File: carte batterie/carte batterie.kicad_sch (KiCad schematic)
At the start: 11 parts, among them IC1 TPS3711DDCT, J1 Conn_01x02_Pin, J2 Conn_01x02_Pin, J3 Conn_01x01_Pin, Q1 SI3127DV-T1-GE3, U1 ATtiny1616-S

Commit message: new compo
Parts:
- added IC2: TPS54531DDA, SOIC127P600X170-9N, symbol SamacSys_Parts:TPS54531DDA
- R4: value R -> 330
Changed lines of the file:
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@@
       (effects (font (size 1.27 1.27)) (justify left))
     )
-    (property "Value" "R" (at 54.61 104.775 0)
+    (property "Value" "330" (at 54.61 104.775 0)
       (effects (font (size 1.27 1.27)) (justify left))
     )
@@
         )
       )
+    )
+  )
+  (symbol (lib_id "SamacSys_Parts:TPS54531DDA") (at 103.505 129.54 0) (unit 1)
+    (in_bom yes) (on_board yes) (dnp no) (fields_autoplaced)
+    (property "Reference" "IC2" (at 118.745 121.92 0)
+      (effects (font (size 1.27 1.27)))
+    )
+    (property "Value" "TPS54531DDA" (at 118.745 124.46 0)
+      (effects (font (size 1.27 1.27)))
+    )
+    (property "Footprint" "SOIC127P600X170-9N" (at 130.175 224.46 0)
+      (effects (font (size 1.27 1.27)) (justify left top) hide)
+    )
+    (property "Datasheet" "http://www.ti.com/lit/gpn/tps54531" (at 130.175 324.46 0)
+      (effects (font (size 1.27 1.27)) (justify left top) hide)
+    )
+    (property "Height" "1.7" (at 130.175 524.46 0)
+      (effects (font (size 1.27 1.27)) (justify left top) hide)
+    )
+    (property "Manufacturer_Name" "Texas Instruments" (at 130.175 624.46 0)
+      (effects (font (size 1.27 1.27)) (justify left top) hide)
+    )
+    (property "Manufacturer_Part_Number" "TPS54531DDA" (at 130.175 724.46 0)
+      (effects (font (size 1.27 1.27)) (justify left top) hide)
+    )
+    (property "Mouser Part Number" "595-TPS54531DDA" (at 130.175 824.46 0)
+      (effects (font (size 1.27 1.27)) (justify left top) hide)
+    )
+    (property "Mouser Price/Stock" "https://www.mouser.co.uk/ProductDetail/Texas-Instruments/TPS54531DDA?qs=jA5Ki6243omoJVKISZs%2FBg%3D%3D" (at 130.175 924.46 0)
+      (effects (font (size 1.27 1.27)) (justify left top) hide)
+    )
+    (property "Arrow Part Number" "TPS54531DDA" (at 130.175 1024.46 0)
+      (effects (font (size 1.27 1.27)) (justify left top) hide)
+    )
+    (property "Arrow Price/Stock" "https://www.arrow.com/en/products/tps54531dda/texas-instruments?region=nac" (at 130.175 1124.46 0)
+      (effects (font (size 1.27 1.27)) (justify left top) hide)
+    )
+    (pin "1")
+    (pin "2")
+    (pin "3")
+    (pin "4")
+    (pin "5")
+    (pin "6")
+    (pin "7")
+    (pin "8")
+    (pin "9")
+    (instances
+      (project "carte batterie"
+        (path "/8afff8df-3578-4f51-814d-4ef430aba141"
+          (reference "IC2") (unit 1)
+        )
+      )

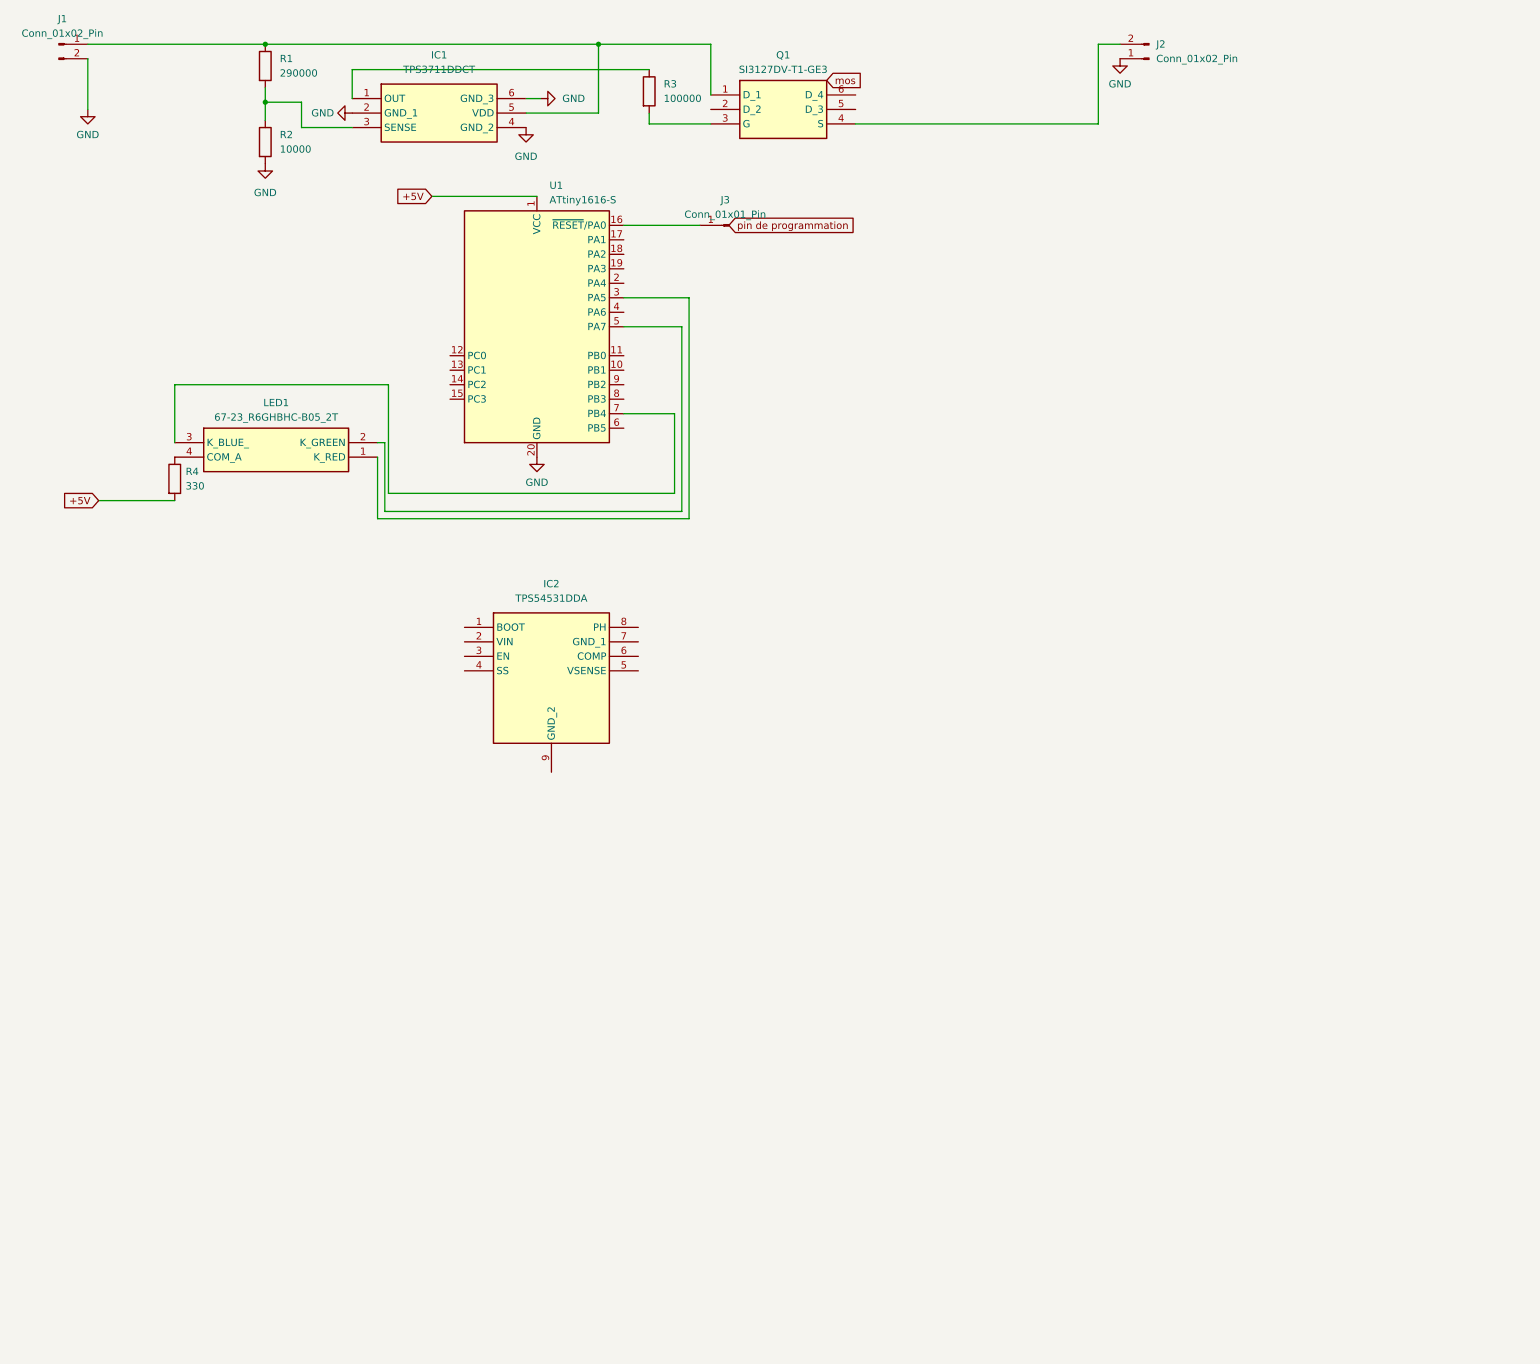
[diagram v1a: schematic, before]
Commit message: ajout ref carte batterie
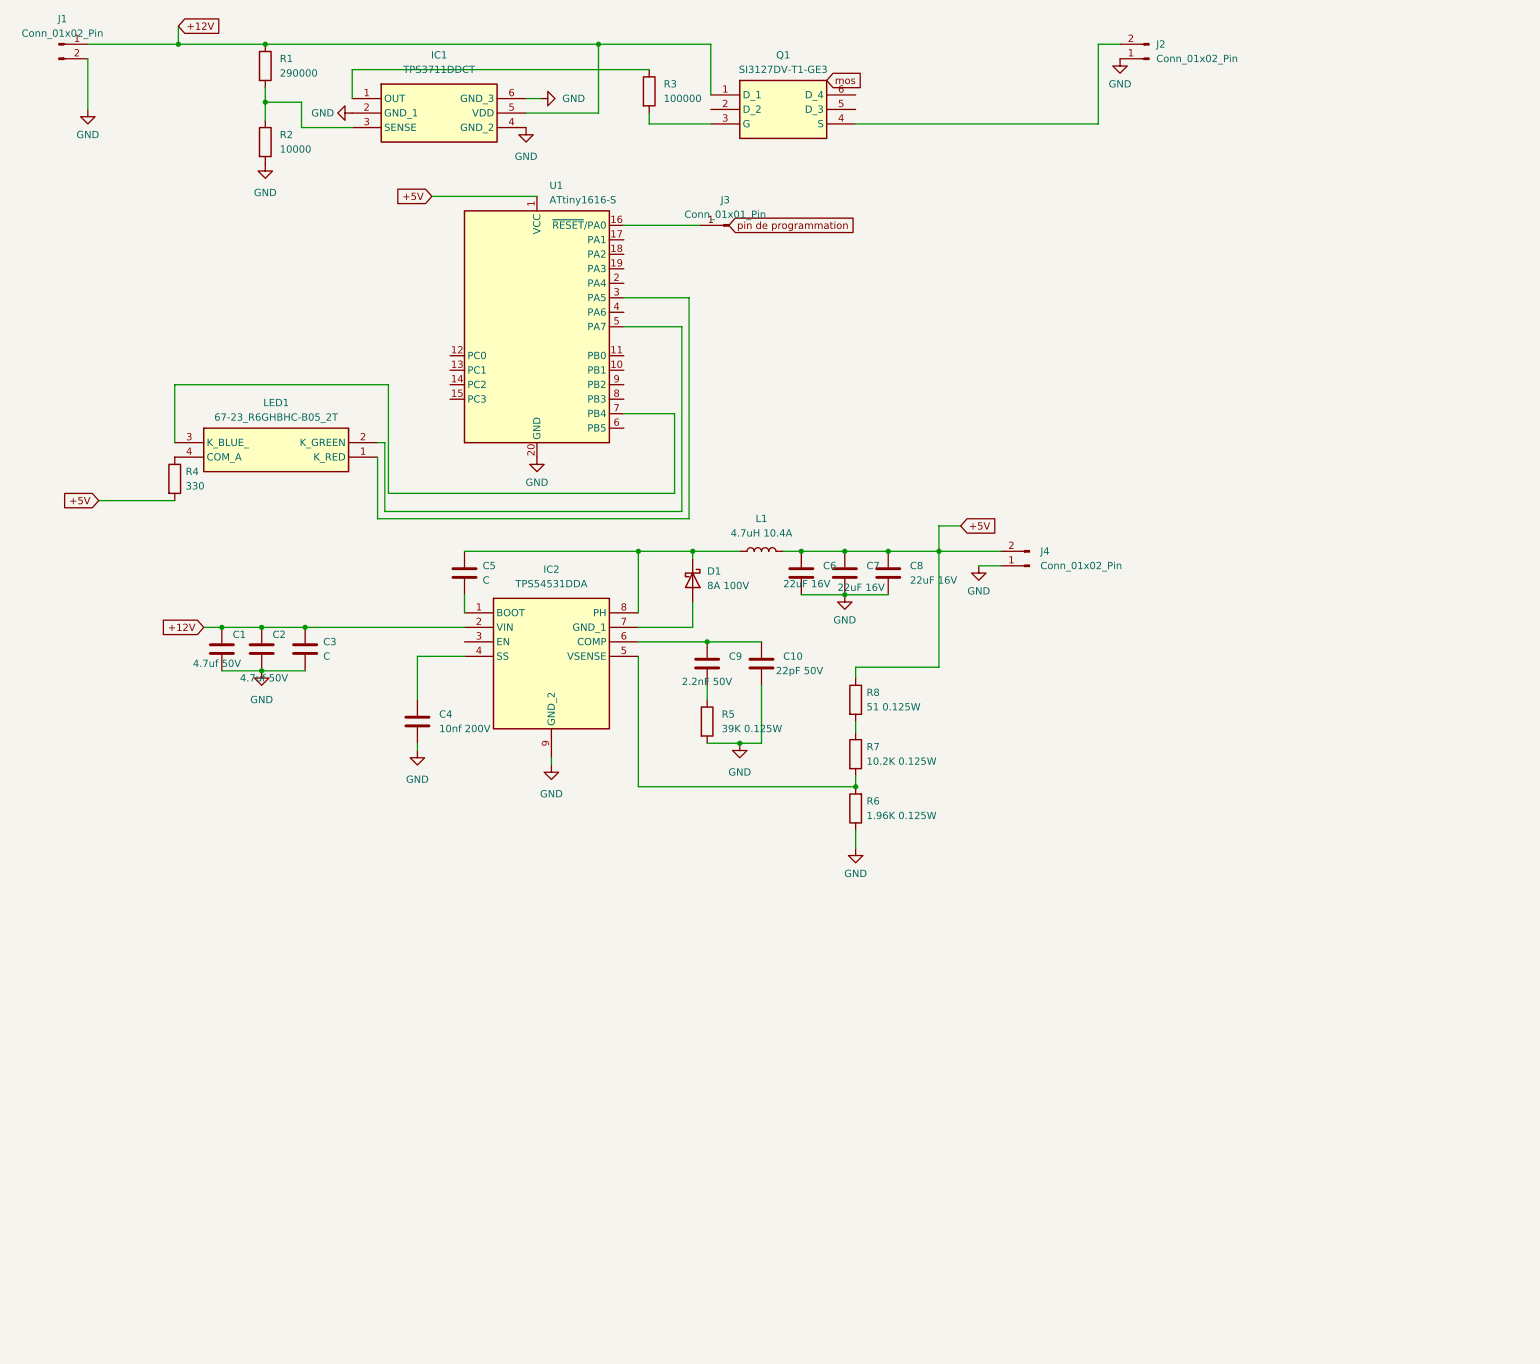
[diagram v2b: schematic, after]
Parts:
- added C1, C2: 4.7uf 50V, Capacitor_SMD:C_0805_2012Metric, symbol Device:C
- added C10: 22pF 50V, Capacitor_SMD:C_0805_2012Metric, symbol Device:C
- added C3, C5: C, symbol Device:C
- added C4: 10nf 200V, Capacitor_SMD:C_0805_2012Metric, symbol Device:C
- added C6, C7, C8: 22uF 16V, Capacitor_SMD:C_0805_2012Metric, symbol Device:C
- added C9: 2.2nF 50V, Capacitor_SMD:C_0603_1608Metric, symbol Device:C
- added D1: 8A 100V, Package_TO_SOT_SMD:TO-277A, symbol Device:D_Schottky
- added J4: Conn_01x02_Pin, symbol Connector:Conn_01x02_Pin
- added L1: 4.7uH 10.4A, Inductor_SMD:L_Wuerth_HCI-1040, symbol Device:L
- added R5: 39K 0.125W, Capacitor_SMD:C_0805_2012Metric, symbol Device:R
- added R6: 1.96K 0.125W, Capacitor_SMD:C_0805_2012Metric, symbol Device:R
- added R7: 10.2K 0.125W, Capacitor_SMD:C_0805_2012Metric, symbol Device:R
- added R8: 51 0.125W, Resistor_SMD:R_0805_2012Metric, symbol Device:R
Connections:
- net +5V: now also C6.1, C7.1, C8.1, J4.2 (Pin_2), L1.2, R8.1
- net GND: now also IC2.9 (GND_2), C1.2, C10.2, C2.2, C3.2, C4.2, C6.2, C7.2, C8.2, J4.1 (Pin_1), R5.2, R6.1
- net +12V: now reaches IC1.5 (VDD), J1.1 (Pin_1), Q1.1 (D_1), R1.1
- net +12V: now also IC2.2 (VIN), C1.1, C2.1, C3.1
- net at IC2.1 (BOOT): now also C5.2
- net at IC2.4 (SS): now also C4.1
- net at IC2.5 (VSENSE): now also R6.2, R7.2
- net at IC2.6 (COMP): now also C10.1, C9.1
- net at IC2.7 (GND_1): now also D1.2 (A)
- net at IC2.8 (PH): now also C5.1, D1.1 (K), L1.1
- new net: C9.2, R5.1
- new net: R7.1, R8.2
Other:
- moved on the sheet: IC2

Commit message: modif
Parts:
- removed J4: Conn_01x02_Pin, symbol Connector:Conn_01x02_Pin
- added J4: RJ11, symbol RJ11:RJ11
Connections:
- net +5V: now also J4.5
- net GND: now also J4.6
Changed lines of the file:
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@@
     (stroke (width 0) (type default))
   )
-  (wire (pts (xy 193.675 118.745) (xy 197.485 118.745))
+  (wire (pts (xy 193.675 118.745) (xy 205.105 118.745))
     (stroke (width 0) (type default))
   )
@@
     (stroke (width 0) (type default))
   )
-  (wire (pts (xy 186.69 116.205) (xy 197.485 116.205))
+  (wire (pts (xy 186.69 116.205) (xy 205.105 116.205))
     (stroke (width 0) (type default))
   )
@@
     )
   )
-  (symbol (lib_id "Connector:Conn_01x02_Pin") (at 202.565 118.745 180) (unit 1)
-    (in_bom yes) (on_board yes) (dnp no) (fields_autoplaced)
-    (property "Reference" "J4" (at 204.47 116.205 0)
-      (effects (font (size 1.27 1.27)) (justify right))
-    )
-    (property "Value" "Conn_01x02_Pin" (at 204.47 118.745 0)
-      (effects (font (size 1.27 1.27)) (justify right))
-    )
-    (property "Footprint" "" (at 202.565 118.745 0)
-      (effects (font (size 1.27 1.27)) hide)
-    )
-    (property "Datasheet" "~" (at 202.565 118.745 0)
-      (effects (font (size 1.27 1.27)) hide)
+  (symbol (lib_id "RJ11:RJ11") (at 207.645 111.125 0) (unit 1)
+    (in_bom yes) (on_board yes) (dnp no) (fields_autoplaced)
+    (property "Reference" "J4" (at 216.535 111.125 0)
+      (effects (font (size 1.27 1.27)) (justify left))
+    )
+    (property "Value" "RJ11" (at 216.535 113.665 0)
+      (effects (font (size 1.27 1.27)) (justify left))
+    )
+    (property "Footprint" "" (at 207.645 111.125 0)
+      (effects (font (size 1.27 1.27)) hide)
+    )
+    (property "Datasheet" "" (at 207.645 111.125 0)
+      (effects (font (size 1.27 1.27)) hide)
+    )
+    (property "MF" "" (at 207.645 111.125 0)
+      (effects (font (size 1.27 1.27)) (justify bottom) hide)
+    )
+    (property "Description" "\n" (at 207.645 111.125 0)
+      (effects (font (size 1.27 1.27)) (justify bottom) hide)
+    )
+    (property "Package" "" (at 207.645 111.125 0)
+      (effects (font (size 1.27 1.27)) (justify bottom) hide)
+    )
+    (property "Price" "" (at 207.645 111.125 0)
+      (effects (font (size 1.27 1.27)) (justify bottom) hide)
+    )
+    (property "SnapEDA_Link" "" (at 207.645 111.125 0)
+      (effects (font (size 1.27 1.27)) (justify bottom) hide)
+    )
+    (property "MP" "" (at 207.645 111.125 0)
+      (effects (font (size 1.27 1.27)) (justify bottom) hide)
+    )
+    (property "Availability" "" (at 207.645 111.125 0)
+      (effects (font (size 1.27 1.27)) (justify bottom) hide)
+    )
+    (property "Check_prices" "" (at 207.645 111.125 0)
+      (effects (font (size 1.27 1.27)) (justify bottom) hide)
     )
     (pin "1")
     (pin "2")
-    (instances
-      (project "carte batterie"
+    (pin "3")
+    (pin "4")
+    (pin "5")
+    (pin "6")
+    (instances
+      (project "carte batterie"

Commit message: carte bat
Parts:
- removed J2: Conn_01x02_Pin, symbol Connector:Conn_01x02_Pin
- removed J3: Conn_01x01_Pin, symbol Connector:Conn_01x01_Pin
- removed J4: RJ11, symbol RJ11:RJ11
- removed U1: ATtiny1616-S, Package_SO:SOIC-20W_7.5x12.8mm_P1.27mm, symbol MCU_Microchip_ATtiny:ATtiny1616-S
- added C11, C12, C13: 4.7uf 50V, Capacitor_SMD:C_0805_2012Metric, symbol Device:C
- added C14: 10nf 200V, Capacitor_SMD:C_0805_2012Metric, symbol Device:C
- added C15: 100nF, symbol Device:C
- added C16: 2.2nF 50V, Capacitor_SMD:C_0603_1608Metric, symbol Device:C
- added C17: 22pF 50V, Capacitor_SMD:C_0805_2012Metric, symbol Device:C
- added C18, C19, C20: 22uF 16V, Capacitor_SMD:C_0805_2012Metric, symbol Device:C
- added D2: 8A 100V, Package_TO_SOT_SMD:TO-277A, symbol Device:D_Schottky
- added IC3: TPS54531DDA, SOIC127P600X170-9N, symbol SamacSys_Parts:TPS54531DDA
- added J2, J3, J4, J5: 110990030, symbol 110990030:110990030
- added J6: Conn_01x02_Pin, symbol Connector:Conn_01x02_Pin
- added L2: 4.7uH 10.4A, Inductor_SMD:L_Wuerth_HCI-1040, symbol Device:L
- added R10: 51 0.125W, Resistor_SMD:R_0805_2012Metric, symbol Device:R
- added R11: 10.2K 0.125W, Capacitor_SMD:C_0805_2012Metric, symbol Device:R
- added R12: 1.96K 0.125W, Capacitor_SMD:C_0805_2012Metric, symbol Device:R
- added R13: 30000, symbol Device:R
- added R14: 10000, symbol Device:R
- added R9: 39K 0.125W, Capacitor_SMD:C_0805_2012Metric, symbol Device:R
- added U2: NUCLEO-F303K8, symbol NUCLEO-F303K8:NUCLEO-F303K8
- added U3: MCP2551-I-P, Package_DIP:DIP-8_W7.62mm, symbol Interface_CAN_LIN:MCP2551-I-P
- C3: value C -> 4.7uf 50V; footprint (none) -> Capacitor_SMD:C_0805_2012Metric
- C5: value C -> 100nF
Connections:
- net +12V: now also C11.1, C12.1, C13.1, IC3.2 (VIN), J6.1 (Pin_1)
- net +5V: now also J3.2, J5.2, U2.4_1 (VIN), U3.3 (VDD)
- net GND: now also C11.2, C12.2, C13.2, C14.2, C17.2, C18.2, C19.2, C20.2, IC3.9 (GND_2), J2.1, J3.1, J4.1, J5.1, J6.2 (Pin_2), R12.1, R14.2, R9.2, U2.3_4 (GND_1), U2.4_2 (GND_2), U3.2 (VSS), U3.8 (Rs)
- net at LED1.1 (K_RED): now also U2.3_6 (PB0)
- net at LED1.2 (K_GREEN): now also U2.3_9 (PB1)
- net at LED1.3 (K_BLUE_): now also U2.3_15 (PB4)
- net at Q1.4 (S): now also J2.2, R13.1
- new net: R13.2, R14.1, U2.4_6 (PA7)
- new net: C16.1, C17.1, IC3.6 (COMP)
- new net: C16.2, R9.1
- new net: C15.2, IC3.1 (BOOT)
- new net: C14.1, IC3.4 (SS)
- new net: IC3.5 (VSENSE), R11.2, R12.2
- new net: D2.2 (A), IC3.7 (GND_1)
- new net: C15.1, D2.1 (K), IC3.8 (PH), L2.1
- new net: J3.4, J5.4, U3.6 (CANL)
- new net: J3.3, J5.3, U3.7 (CANH)
- new net: R10.2, R11.1
- new net +5Vn2: C18.1, C19.1, C20.1, J4.2, L2.2, R10.1
- new net cand: U2.3_5 (PA12), U3.1 (TXD)
- new net canr: U2.3_13 (PA11), U3.4 (RXD)
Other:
- moved on the sheet: C1, C10, C2, C4, C5, C6, C7, C8, C9, D1, IC2, L1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

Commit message: carte bat
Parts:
- removed C11, C12, C13: 4.7uf 50V, Capacitor_SMD:C_0805_2012Metric, symbol Device:C
- removed C14: 10nf 200V, Capacitor_SMD:C_0805_2012Metric, symbol Device:C
- removed C15: 100nF, symbol Device:C
- removed C16: 2.2nF 50V, Capacitor_SMD:C_0603_1608Metric, symbol Device:C
- removed C17: 22pF 50V, Capacitor_SMD:C_0805_2012Metric, symbol Device:C
- removed C18, C19, C20: 22uF 16V, Capacitor_SMD:C_0805_2012Metric, symbol Device:C
- removed D2: 8A 100V, Package_TO_SOT_SMD:TO-277A, symbol Device:D_Schottky
- removed IC3: TPS54531DDA, SOIC127P600X170-9N, symbol SamacSys_Parts:TPS54531DDA
- removed J2, J3, J4, J5: 110990030, symbol 110990030:110990030
- removed J6: Conn_01x02_Pin, symbol Connector:Conn_01x02_Pin
- removed L2: 4.7uH 10.4A, Inductor_SMD:L_Wuerth_HCI-1040, symbol Device:L
- removed R10: 51 0.125W, Resistor_SMD:R_0805_2012Metric, symbol Device:R
- removed R11: 10.2K 0.125W, Capacitor_SMD:C_0805_2012Metric, symbol Device:R
- removed R12: 1.96K 0.125W, Capacitor_SMD:C_0805_2012Metric, symbol Device:R
- removed R13: 30000, symbol Device:R
- removed R14: 10000, symbol Device:R
- removed U2: NUCLEO-F303K8, symbol NUCLEO-F303K8:NUCLEO-F303K8
- removed U3: MCP2551-I-P, Package_DIP:DIP-8_W7.62mm, symbol Interface_CAN_LIN:MCP2551-I-P
- added J2: Conn_01x02_Pin, symbol Connector:Conn_01x02_Pin
- added J3: Conn_01x01_Pin, symbol Connector:Conn_01x01_Pin
- added J4: RJ11, symbol RJ11:RJ11
- added U1: ATtiny1616-S, Package_SO:SOIC-20W_7.5x12.8mm_P1.27mm, symbol MCU_Microchip_ATtiny:ATtiny1616-S
- C5: value 100nF -> C
- R1: value 290000 -> 290k
- R2: value 10000 -> 10k
- R3: value 100000 -> 100k
- R9: value 39K 0.125W -> 1M; footprint Capacitor_SMD:C_0805_2012Metric -> (none)
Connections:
- net +12V: now also Q1.6 (D_4), R9.1; no longer Q1.1 (D_1)
- net +5V: now also J4.5, U1.1 (VCC)
- net GND: now also J2.1 (Pin_1), J4.6, U1.20 (GND); no longer R9.2
- net at Q1.3 (G), R3.2: now also R9.2
- net at LED1.1 (K_RED): now also U1.3 (PA5)
- net at LED1.2 (K_GREEN): now also U1.5 (PA7)
- net at LED1.3 (K_BLUE_): now also U1.7 (PB4)
- new net: J3.1 (Pin_1), U1.16 (~{RESET}/PA0)
- new net: J2.2 (Pin_2), Q1.1 (D_1)
- new net CS: U1.2 (PA4)
- new net MISO: U1.18 (PA2)
- new net MOSI: U1.17 (PA1)
- new net SCK: U1.19 (PA3)
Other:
- moved on the sheet: C1, C10, C2, C4, C5, C6, C7, C8, C9, D1, IC2, L1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
